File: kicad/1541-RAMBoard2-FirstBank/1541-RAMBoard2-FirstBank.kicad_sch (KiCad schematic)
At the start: 12 parts, among them J1 Conn_01x02_Male, U1 27C512, U2 74LS139, U3 KM62256CLP, U4_SOCKET1 27128

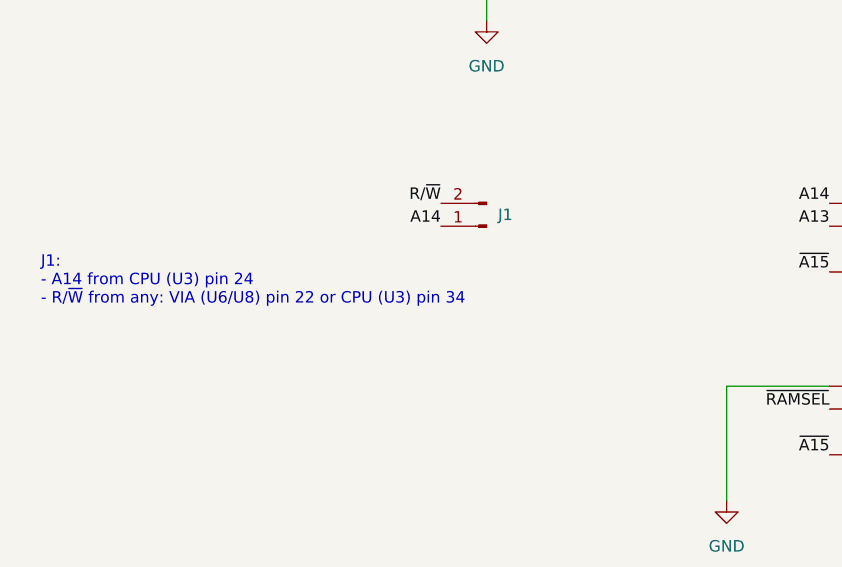
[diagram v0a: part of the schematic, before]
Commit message: revision 1.1 - no changes except messages that R/W has to be connected to RAM (U6) R/W from gate array (U10), not directly to CPU R/W
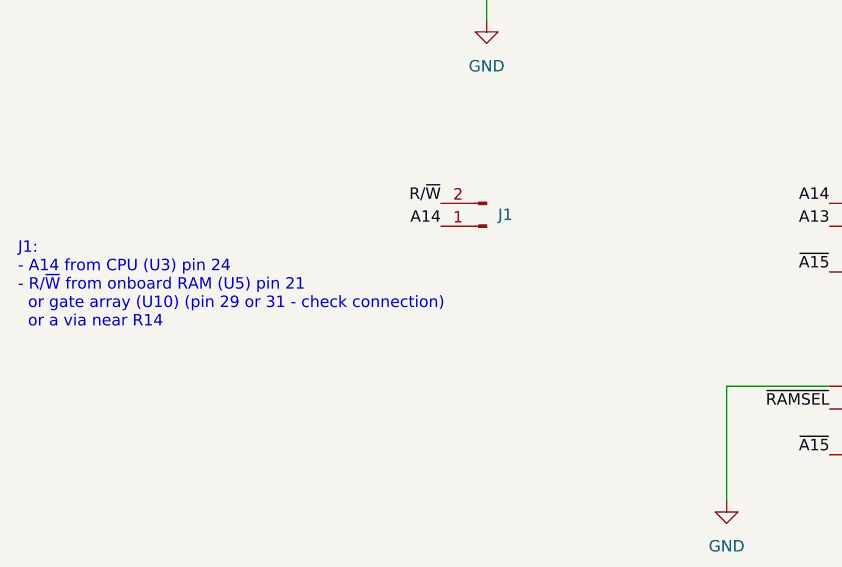
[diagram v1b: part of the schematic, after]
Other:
- note added: "J1: - A14 from CPU (U3) pin 24 - R/~{W} from onboard RAM (U5) pin 21 or gate array (U10) (pin 29 or 31 - check connection) or a via near R14"
- note removed: "J1: - A14 from CPU (U3) pin 24 - R/~{W} from any: VIA (U6/U8) pin 22 or CPU (U3) pin 34"
- title: RAMBoard ][: First Bank -> RAMBoard ][
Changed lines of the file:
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@@
   (paper "A4")
   (title_block
-    (title "RAMBoard ][: First Bank")
-    (date "2024-03-21")
-    (rev "1")
+    (title "RAMBoard ][")
+    (date "2024-04-20")
+    (rev "2")
     (company "YTM Enterprises")
     (comment 1 "Maciej Witkowiak, <ytm@elysium.pl>")
@@
     (effects (font (size 1.27 1.27)) (justify left bottom))
   )
-  (text "J1:\n- A14 from CPU (U3) pin 24\n- R/~{W} from any: VIA (U6/U8) pin 22 or CPU (U3) pin 34\n"
-    (at 22.86 143.51 0)
+  (text "J1:\n- A14 from CPU (U3) pin 24\n- R/~{W} from onboard RAM (U5) pin 21\n  or gate array (U10) (pin 29 or 31 - check connection)\n  or a via near R14"
+    (at 20.32 146.05 0)
     (effects (font (size 1.27 1.27)) (justify left bottom))
   )
